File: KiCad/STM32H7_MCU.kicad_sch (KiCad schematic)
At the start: 51 parts, among them IC2 SN74LVC1G14DBVR, IC3 STM32H7R7L8H6H, IC4 TLV75718PDRVR, Y1 VXM7-9032-25M0000000

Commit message: BOM update
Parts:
- C4, C5: DigiKey (none) -> 490-7299-1-ND; Mouser (none) -> 81-GRM1555C2A100JA1D; TME (none) -> GRM1555C1H100GA01D
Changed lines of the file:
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@@
 			)
 		)
-		(property "TME" ""
+		(property "TME" "GRM1555C1H100GA01D"
 			(at 142.24 132.08 0)
 			(effects
@@
 			)
 		)
-		(property "DigiKey" ""
+		(property "DigiKey" "490-7299-1-ND"
 			(at 142.24 132.08 0)
 			(effects
@@
 			)
 		)
-		(property "Mouser" ""
+		(property "Mouser" "81-GRM1555C2A100JA1D"
 			(at 142.24 132.08 0)
 			(effects
@@
 			)
 		)
-		(property "TME" ""
+		(property "TME" "GRM1555C1H100GA01D"
 			(at 142.24 142.24 0)
 			(effects
@@
 			)
 		)
-		(property "DigiKey" ""
+		(property "DigiKey" "490-7299-1-ND"
 			(at 142.24 142.24 0)
 			(effects
@@
 			)
 		)
-		(property "Mouser" ""
+		(property "Mouser" "81-GRM1555C2A100JA1D"
 			(at 142.24 142.24 0)
 			(effects

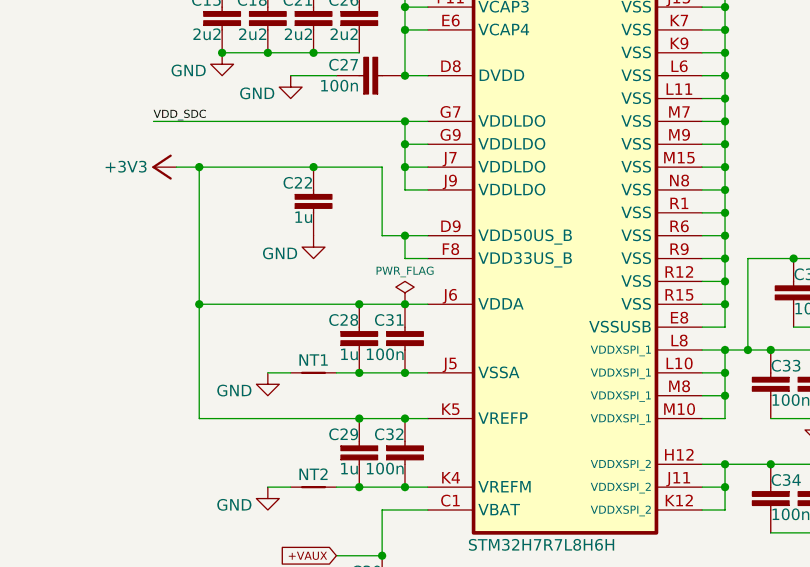
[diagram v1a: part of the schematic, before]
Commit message: TFT_DVID control signals on 1:2 video mux removed
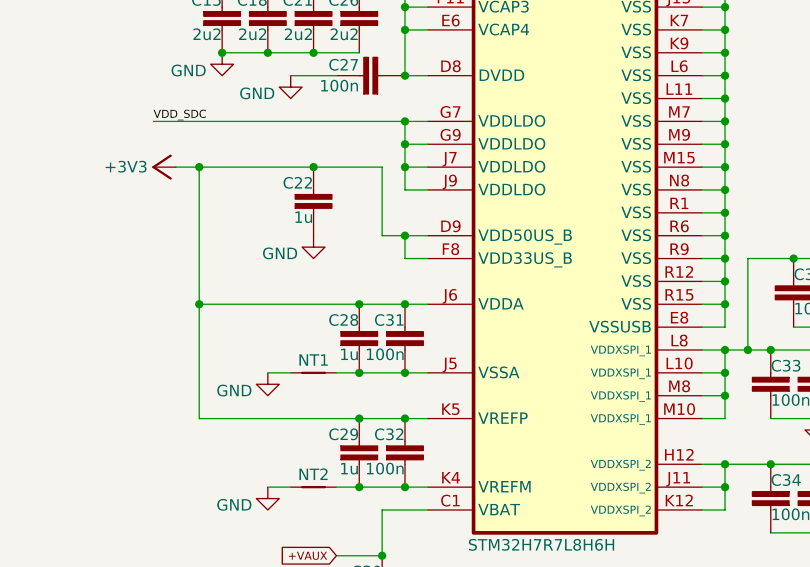
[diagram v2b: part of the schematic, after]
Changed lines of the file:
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@@
 	(title_block
 		(title "${project_name}")
-		(date "2025-11-03")
+		(date "2025-11-17")
 		(rev "${project_version}")
 		(company "${project_creator}")
@@
 					(unit 1)
 				)
-			)
-		)
-	)
-	(symbol
-		(lib_id "power:PWR_FLAG")
-		(at 213.36 114.3 0)
-		(unit 1)
-		(exclude_from_sim no)
-		(in_bom yes)
-		(on_board yes)
-		(dnp no)
-		(property "Reference" "#FLG05"
-			(at 213.36 112.395 0)
-			(effects
-				(font
-					(size 1.27 1.27)
-				)
-				(hide yes)
-			)
-		)
-		(property "Value" "PWR_FLAG"
-			(at 213.36 111.125 0)
-			(effects
-				(font
-					(size 0.889 0.889)
-				)
-				(justify bottom)
-			)
-		)
-		(property "Footprint" ""
-			(at 213.36 114.3 0)
-			(effects
-				(font
-					(size 1.27 1.27)
-				)
-				(hide yes)
-			)
-		)
-		(property "Datasheet" "~"
-			(at 213.36 114.3 0)
-			(effects
-				(font
-					(size 1.27 1.27)
-				)
-				(hide yes)
-			)
-		)
-		(property "Description" "Special symbol for telling ERC where power comes from"
-			(at 213.36 114.3 0)
-			(effects
-				(font
-					(size 1.27 1.27)
-				)
-				(hide yes)
-			)
-		)
-		(pin "1"
-		)
-		(instances
-			(project "BB3plus CM5 STM32H7 module"
-				(path "/1a4f0aea-3a69-423f-8790-3103cd0321c4/d7166dbe-caf3-45a8-82fe-1ff0a9696e25"
-					(reference "#FLG05")
-					(unit 1)
-				)
